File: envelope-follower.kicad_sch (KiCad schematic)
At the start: 44 parts, among them U1201 TL072, U1202 TL074

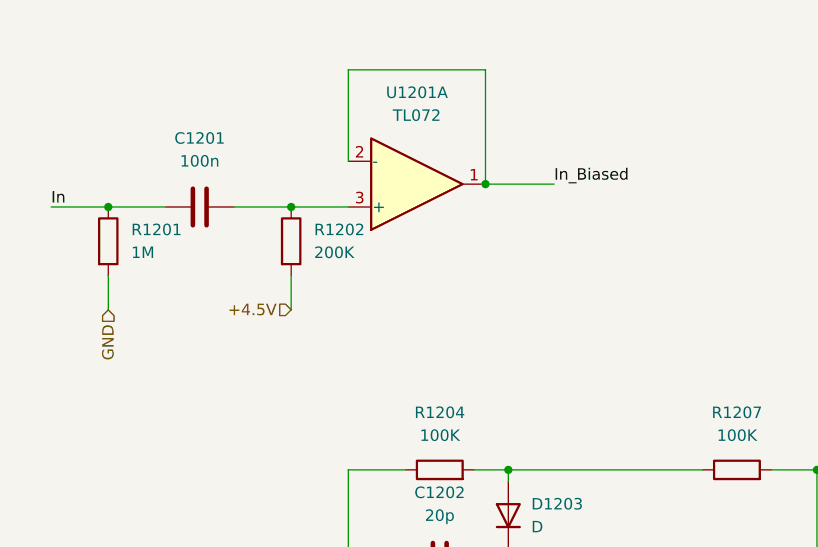
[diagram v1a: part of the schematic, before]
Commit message: Add envelope follower gain stage
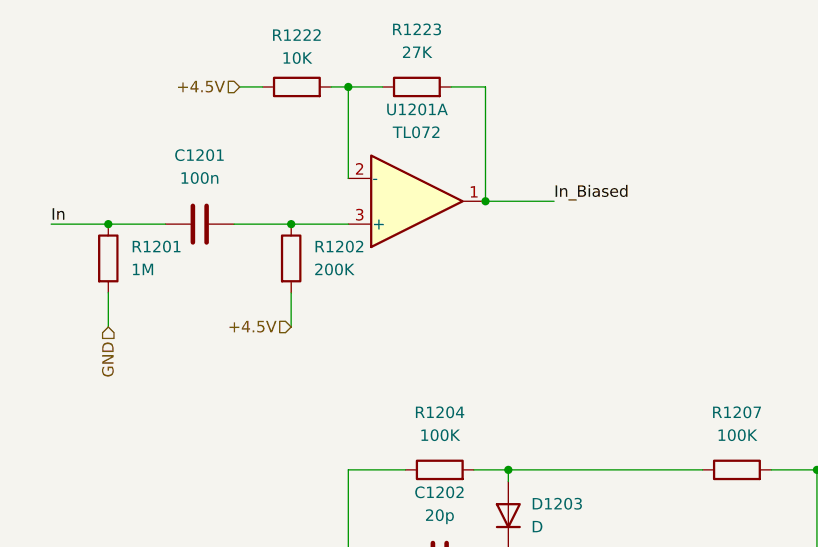
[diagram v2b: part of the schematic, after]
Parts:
- added R1222: 10K, Resistor_SMD:R_0603_1608Metric_Pad0.98x0.95mm_HandSolder, symbol Device:R
- added R1223: 27K, Resistor_SMD:R_0603_1608Metric_Pad0.98x0.95mm_HandSolder, symbol Device:R
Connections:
- net +4.5V: now also R1222.1
- net In_Biased: now also R1223.2; no longer U1201.2 (-)
- new net: R1222.2, R1223.1, U1201.2 (-)
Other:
- moved on the sheet: C1201, R1201, R1202, U1201A

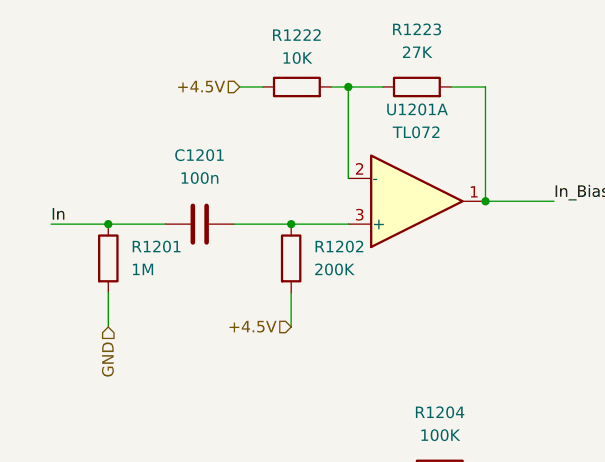
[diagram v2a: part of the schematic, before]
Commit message: Increase the size of dc blocking caps
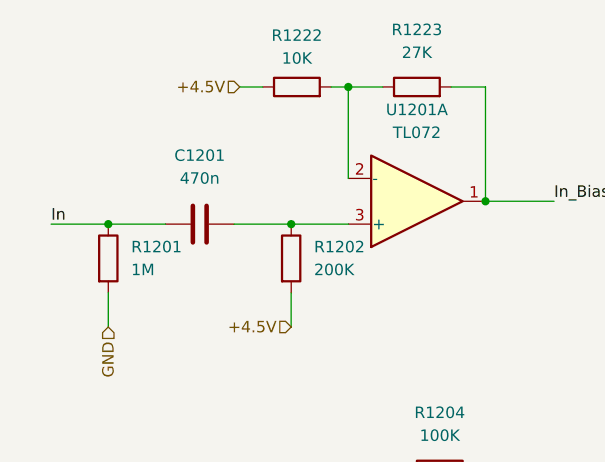
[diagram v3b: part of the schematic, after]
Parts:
- C1201: value 100n -> 470n; footprint Capacitor_SMD:C_0603_1608Metric_Pad1.08x0.95mm_HandSolder -> Capacitor_SMD:C_0805_2012Metric_Pad1.18x1.45mm_HandSolder
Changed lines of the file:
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@@
+    (pin "2")
+  )
+  (symbol (lib_id "Device:C") (at 31.75 34.925 90) (unit 1)
+    (in_bom yes) (on_board yes) (fields_autoplaced)
+    (property "Reference" "C1201" (id 0) (at 31.75 27.305 90))
+    (property "Value" "470n" (id 1) (at 31.75 29.845 90))
+    (property "Footprint" "Capacitor_SMD:C_0805_2012Metric_Pad1.18x1.45mm_HandSolder" (id 2) (at 35.56 33.9598 0)
+      (effects (font (size 1.27 1.27)) hide)
+    )
+    (property "Datasheet" "~" (id 3) (at 31.75 34.925 0)
+      (effects (font (size 1.27 1.27)) hide)
+    )
+    (pin "1")
     (pin "2")
   )
@@
       (effects (font (size 1.27 1.27)) hide)
     )
-    (pin "1")
-    (pin "2")
-  )
-  (symbol (lib_id "Device:C") (at 31.75 34.925 90) (unit 1)
-    (in_bom yes) (on_board yes) (fields_autoplaced)
-    (property "Reference" "C1201" (id 0) (at 31.75 27.305 90))
-    (property "Value" "100n" (id 1) (at 31.75 29.845 90))
-    (property "Footprint" "Capacitor_SMD:C_0603_1608Metric_Pad1.08x0.95mm_HandSolder" (id 2) (at 35.56 33.9598 0)
-      (effects (font (size 1.27 1.27)) hide)
-    )
-    (property "Datasheet" "~" (id 3) (at 31.75 34.925 0)
-      (effects (font (size 1.27 1.27)) hide)
-    )

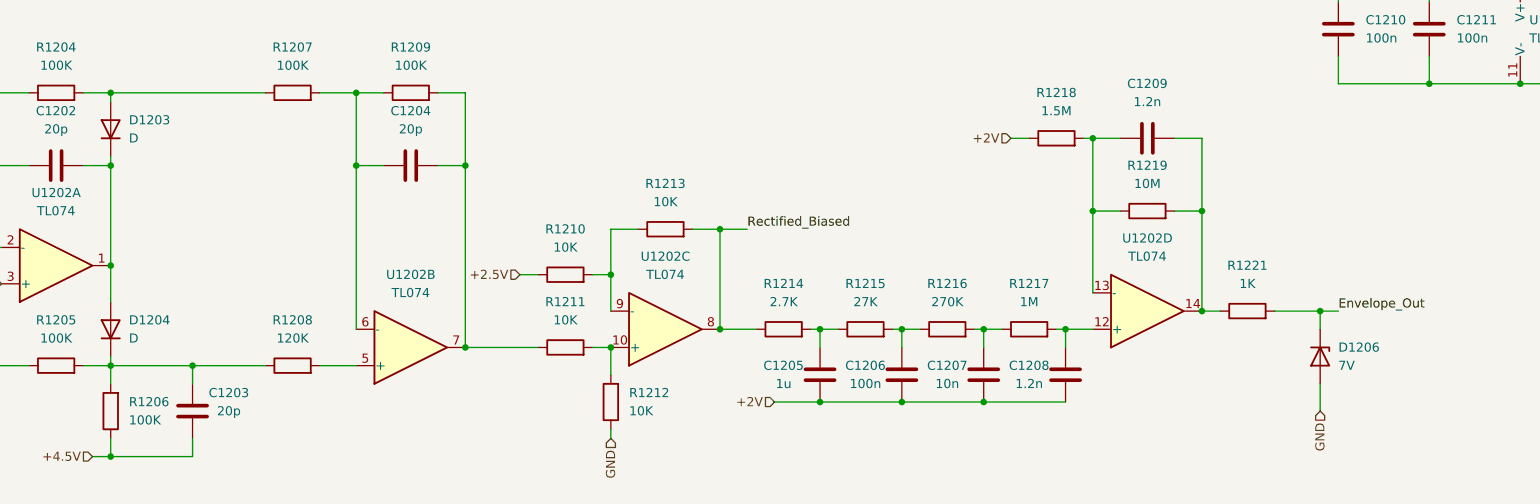
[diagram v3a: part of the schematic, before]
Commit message: Add JLC parts numbers
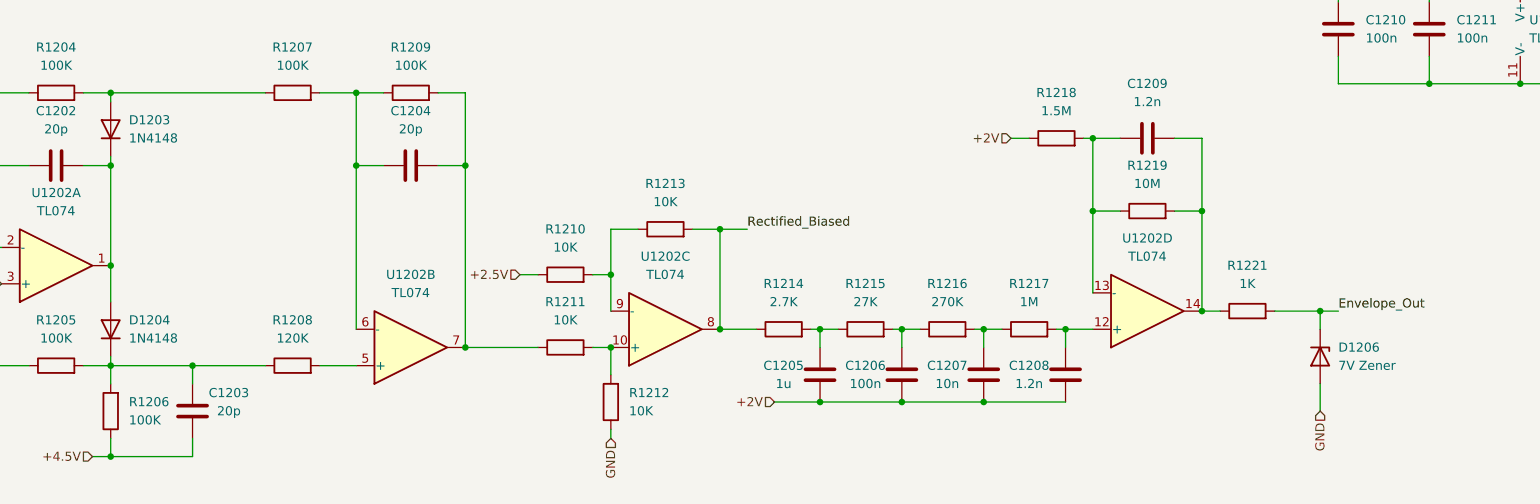
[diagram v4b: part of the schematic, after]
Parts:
- C1201: LCSC (none) -> C651004; Role (none) -> audio-coupling
- C1202, C1203, C1204: LCSC (none) -> C105621; Role (none) -> audio-filter
- C1205: LCSC (none) -> C59302; Role (none) -> cv-filter
- C1206: LCSC (none) -> C519438; Role (none) -> cv-filter
- C1207: LCSC (none) -> C57112; Role (none) -> cv-filter
- C1208, C1209: LCSC (none) -> C342931; Role (none) -> audio-filter
- C1210, C1211: LCSC (none) -> C497032; Role (none) -> ic-bypass
- D1201, D1202, D1205: LCSC (none) -> C20936
- D1203, D1204: value D -> 1N4148; LCSC (none) -> C2128
- D1206: value 7V -> 7V Zener; LCSC (none) -> C5190173
- R1201, R1217: LCSC (none) -> C234360
- R1202: LCSC (none) -> C203392
- R1203, R1210, R1211, R1212, R1213, R1222: LCSC (none) -> C98220
- R1204, R1205, R1206, R1207, R1209: LCSC (none) -> C14675
- R1208: LCSC (none) -> C100737
- R1214: LCSC (none) -> C328353
- R1215, R1223: LCSC (none) -> C116691
- R1216: LCSC (none) -> C2907019
- R1218: LCSC (none) -> C211695
- R1219: LCSC (none) -> C2930145
- R1220, R1221: LCSC (none) -> C2907002
- U1201: LCSC (none) -> C67473
- U1202: LCSC (none) -> C6963
